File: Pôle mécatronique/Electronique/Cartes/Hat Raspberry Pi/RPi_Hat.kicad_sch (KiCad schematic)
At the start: 9 parts, among them J1 Conn_02x03_Odd_Even, U1 XBee, U2 MCP25625-x-SS, Y1 8MHz

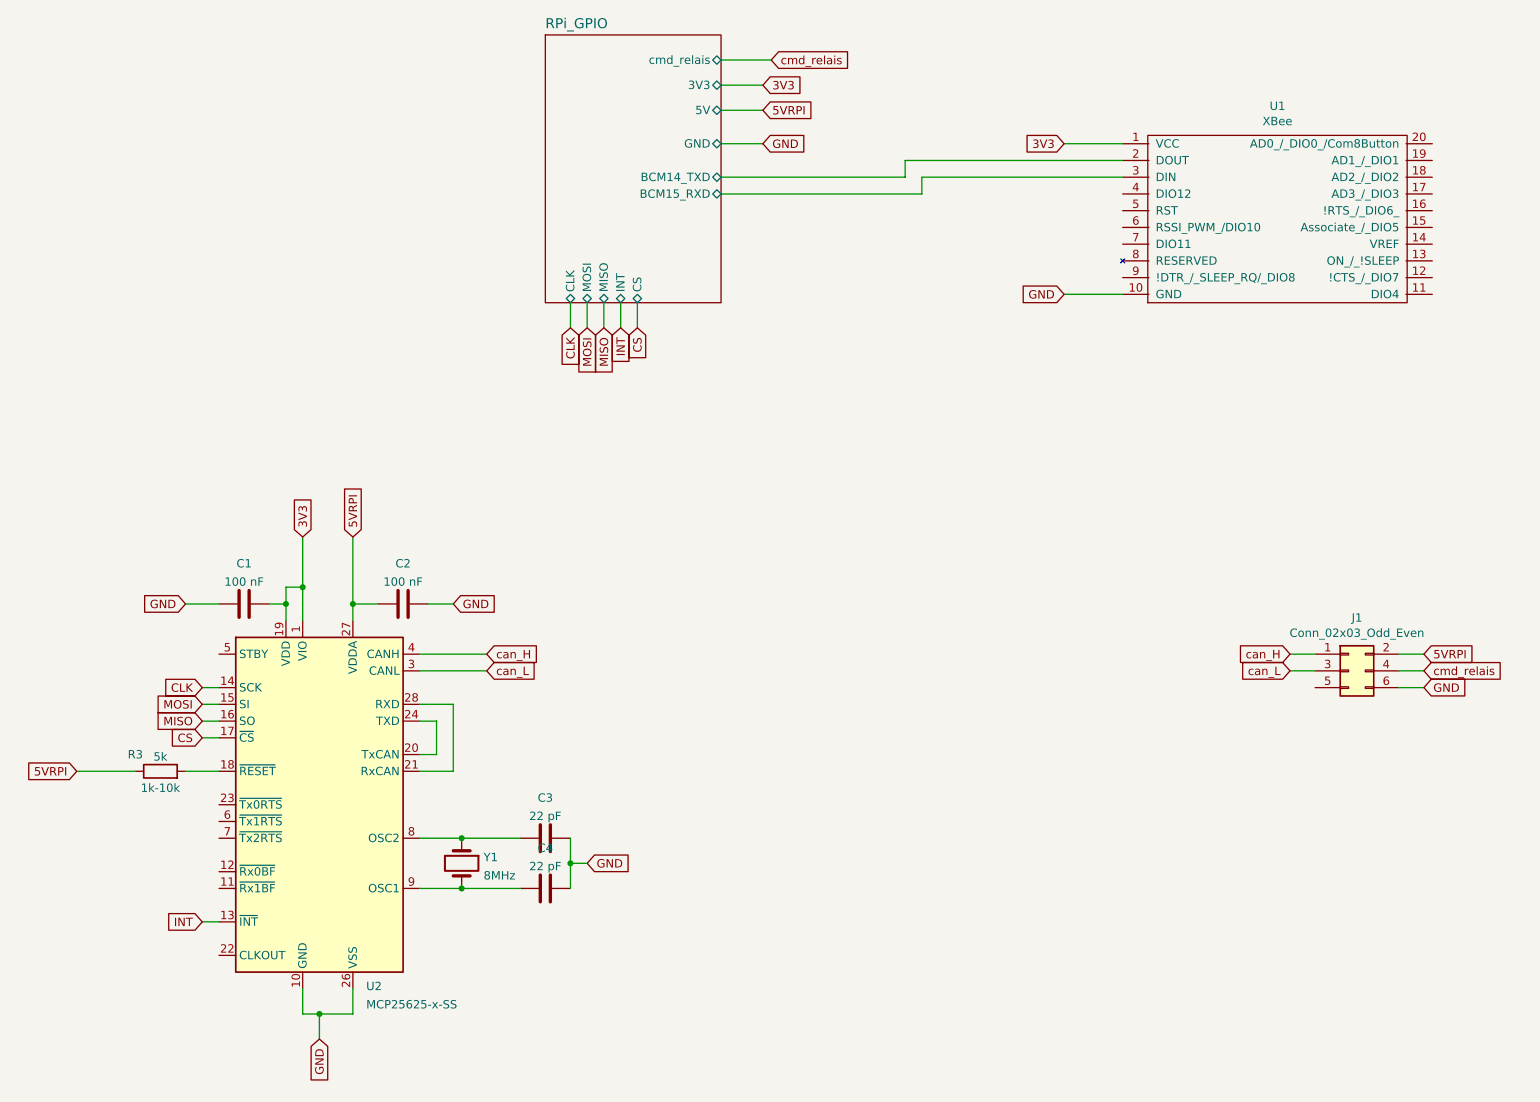
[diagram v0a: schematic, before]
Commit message: Update alim
Corrections pistes et via
Merci Hugo et Francois
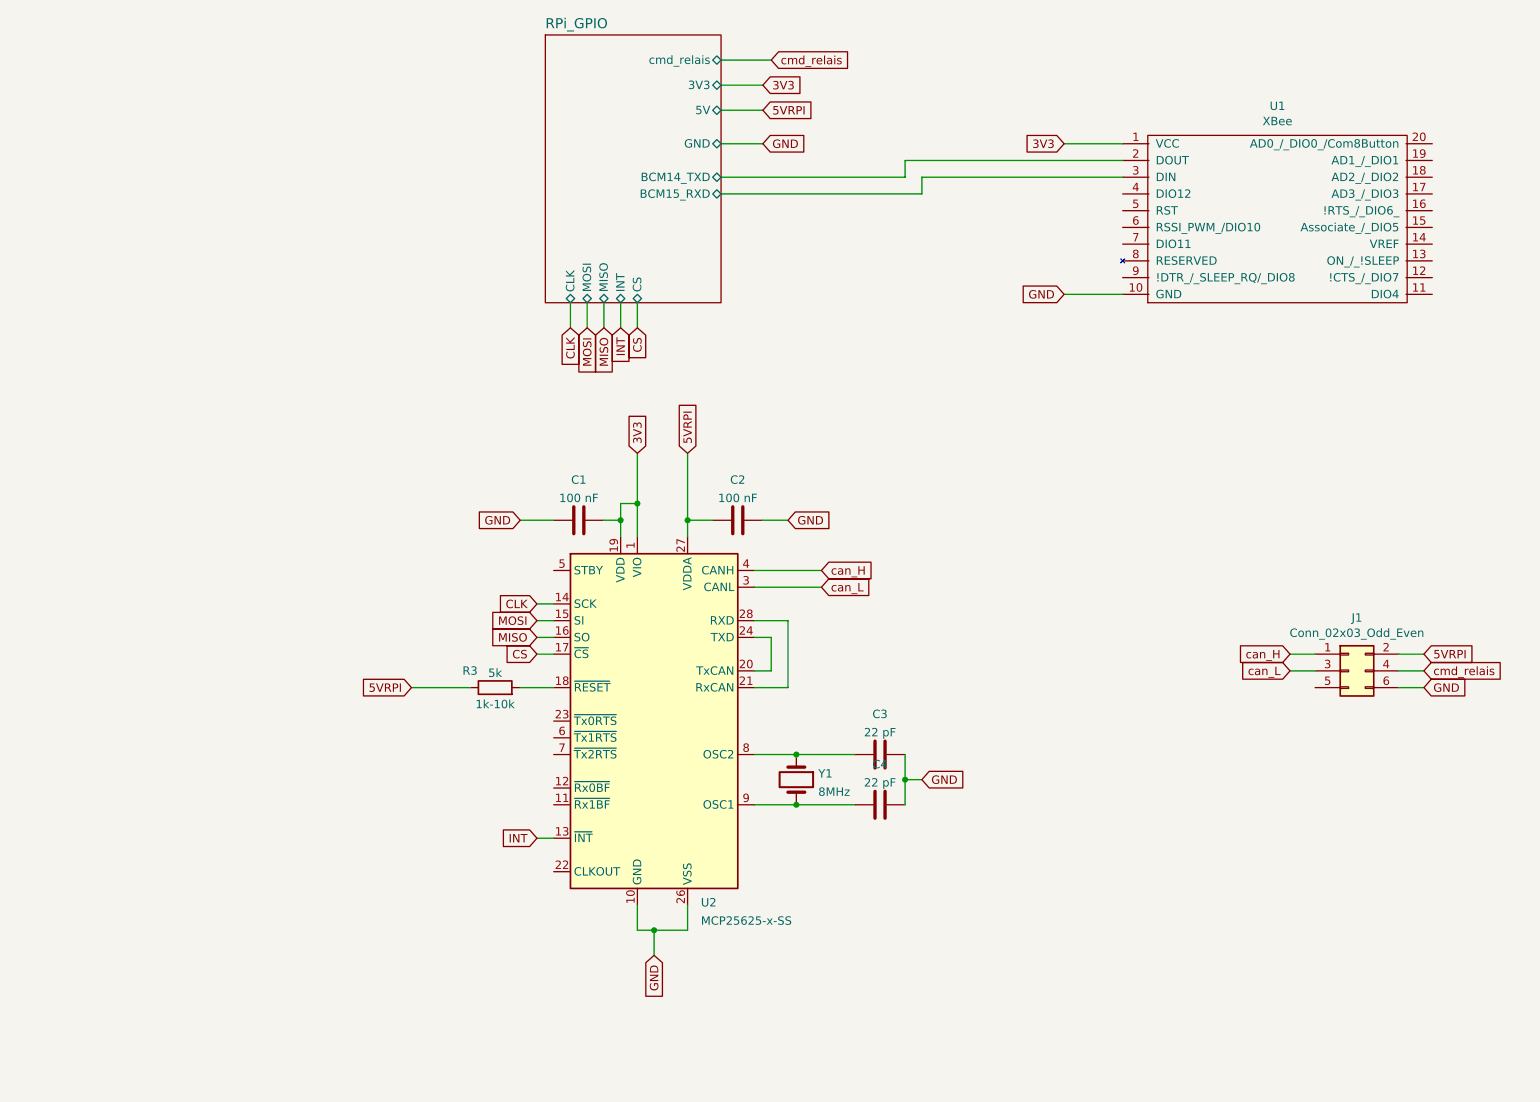
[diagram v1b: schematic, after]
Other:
- moved on the sheet: C1, C2, C3, C4, R3, U2, Y1

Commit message: Update alim correction
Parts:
- added R1: R, Resistor_THT:R_Axial_DIN0207_L6.3mm_D2.5mm_P2.54mm_Vertical, symbol Device:R
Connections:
- net can_H: now also R1.2
- net can_L: now also R1.1
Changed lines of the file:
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@@
   (junction (at 139.7 140.97) (diameter 0) (color 0 0 0 0)
   )
+  (junction (at 201.93 121.92) (diameter 0) (color 0 0 0 0)
+  )
   (junction (at 113.03 105.41) (diameter 0) (color 0 0 0 0)
   )
   (junction (at 118.11 167.64) (diameter 0) (color 0 0 0 0)
   )
+  (junction (at 201.93 129.54) (diameter 0) (color 0 0 0 0)
+  )
   (junction (at 156.21 144.78) (diameter 0) (color 0 0 0 0)
   )
@@
     (stroke (width 0) (type default) (color 0 0 0 0))
   )
+  (wire (pts (xy 201.93 121.92) (xy 209.55 121.92))
+    (stroke (width 0) (type default) (color 0 0 0 0))
+  )
   (wire (pts (xy 113.03 102.87) (xy 115.57 102.87))
     (stroke (width 0) (type default) (color 0 0 0 0))
@@
     (stroke (width 0) (type default) (color 0 0 0 0))
   )
+  (wire (pts (xy 196.85 129.54) (xy 201.93 129.54))
+    (stroke (width 0) (type default) (color 0 0 0 0))
+  )
   (wire (pts (xy 100.33 125.73) (xy 102.87 125.73))
     (stroke (width 0) (type default) (color 0 0 0 0))
@@
     (stroke (width 0) (type default) (color 0 0 0 0))
   )
+  (wire (pts (xy 196.85 121.92) (xy 201.93 121.92))
+    (stroke (width 0) (type default) (color 0 0 0 0))
+  )
   (wire (pts (xy 134.62 105.41) (xy 138.43 105.41))
     (stroke (width 0) (type default) (color 0 0 0 0))
@@
     (stroke (width 0) (type default) (color 0 0 0 0))
   )
+  (wire (pts (xy 209.55 128.27) (xy 209.55 129.54))
+    (stroke (width 0) (type default) (color 0 0 0 0))
+  )
   (wire (pts (xy 123.19 163.83) (xy 123.19 167.64))
     (stroke (width 0) (type default) (color 0 0 0 0))
@@
     (stroke (width 0) (type default) (color 0 0 0 0))
   )
+  (wire (pts (xy 209.55 125.73) (xy 218.44 125.73))
+    (stroke (width 0) (type default) (color 0 0 0 0))
+  )
   (wire (pts (xy 100.33 153.67) (xy 102.87 153.67))
     (stroke (width 0) (type default) (color 0 0 0 0))
@@
     (stroke (width 0) (type default) (color 0 0 0 0))
   )
-  (wire (pts (xy 214.63 128.27) (xy 218.44 128.27))
-    (stroke (width 0) (type default) (color 0 0 0 0))
-  )
   (wire (pts (xy 107.95 72.39) (xy 107.95 76.2))
     (stroke (width 0) (type default) (color 0 0 0 0))
@@
     (stroke (width 0) (type default) (color 0 0 0 0))
   )
+  (wire (pts (xy 218.44 128.27) (xy 209.55 128.27))
+    (stroke (width 0) (type default) (color 0 0 0 0))
+  )
   (wire (pts (xy 135.89 128.27) (xy 133.35 128.27))
     (stroke (width 0) (type default) (color 0 0 0 0))
   )
+  (wire (pts (xy 209.55 121.92) (xy 209.55 125.73))
+    (stroke (width 0) (type default) (color 0 0 0 0))
+  )
   (wire (pts (xy 128.27 48.26) (xy 134.62 48.26))
     (stroke (width 0) (type default) (color 0 0 0 0))
@@
     (stroke (width 0) (type default) (color 0 0 0 0))
   )
-  (wire (pts (xy 214.63 125.73) (xy 218.44 125.73))
-    (stroke (width 0) (type default) (color 0 0 0 0))
-  )
   (wire (pts (xy 123.19 105.41) (xy 127 105.41))
     (stroke (width 0) (type default) (color 0 0 0 0))
@@
   )
   (wire (pts (xy 139.7 140.97) (xy 148.59 140.97))
+    (stroke (width 0) (type default) (color 0 0 0 0))
+  )
+  (wire (pts (xy 201.93 129.54) (xy 209.55 129.54))
     (stroke (width 0) (type default) (color 0 0 0 0))
   )
@@
     )
   )
-  (global_label "can_L" (shape input) (at 214.63 128.27 180) (fields_autoplaced)
-    (effects (font (size 1.27 1.27)) (justify right))
-    (property "Intersheet References" "${INTERSHEET_REFS}" (id 0) (at 189.23 57.15 0)
+  (global_label "can_L" (shape input) (at 196.85 129.54 180) (fields_autoplaced)
+    (effects (font (size 1.27 1.27)) (justify right))
+    (property "Intersheet References" "${INTERSHEET_REFS}" (id 0) (at 171.45 58.42 0)
       (effects (font (size 1.27 1.27)) hide)
     )
@@
     )
   )
-  (global_label "can_H" (shape input) (at 214.63 125.73 180) (fields_autoplaced)
-    (effects (font (size 1.27 1.27)) (justify right))
-    (property "Intersheet References" "${INTERSHEET_REFS}" (id 0) (at 189.23 59.69 0)
+  (global_label "can_H" (shape input) (at 196.85 121.92 180) (fields_autoplaced)
+    (effects (font (size 1.27 1.27)) (justify right))
+    (property "Intersheet References" "${INTERSHEET_REFS}" (id 0) (at 171.45 55.88 0)
       (effects (font (size 1.27 1.27)) hide)
     )
@@
     )
     (property "Description" "1k-10k" (id 4) (at 93.98 133.35 90))
+    (pin "1")
+    (pin "2")
+  )
+  (symbol (lib_id "Device:R") (at 201.93 125.73 180) (unit 1)
+    (in_bom yes) (on_board yes) (fields_autoplaced)
+    (property "Reference" "R1" (id 0) (at 203.708 124.8215 0)
+      (effects (font (size 1.27 1.27)) (justify right))
+    )
+    (property "Value" "R" (id 1) (at 203.708 127.5966 0)
+      (effects (font (size 1.27 1.27)) (justify right))
+    )
+    (property "Footprint" "Resistor_THT:R_Axial_DIN0207_L6.3mm_D2.5mm_P2.54mm_Vertical" (id 2) (at 203.708 125.73 90)
+      (effects (font (size 1.27 1.27)) hide)
+    )
+    (property "Datasheet" "~" (id 3) (at 201.93 125.73 0)
+      (effects (font (size 1.27 1.27)) hide)
+    )
     (pin "1")
     (pin "2")
@@
       (reference "J2") (unit 1) (value "RPi_GPIO") (footprint "RPi_Hat:Pin_Header_Straight_2x20")
     )
+    (path "/5d503d09-3382-41b1-85dd-a984512b456d"
+      (reference "R1") (unit 1) (value "R") (footprint "Resistor_THT:R_Axial_DIN0207_L6.3mm_D2.5mm_P2.54mm_Vertical")
+    )
     (path "/47b96755-77b4-4d1f-b7c7-e83301b841d7"

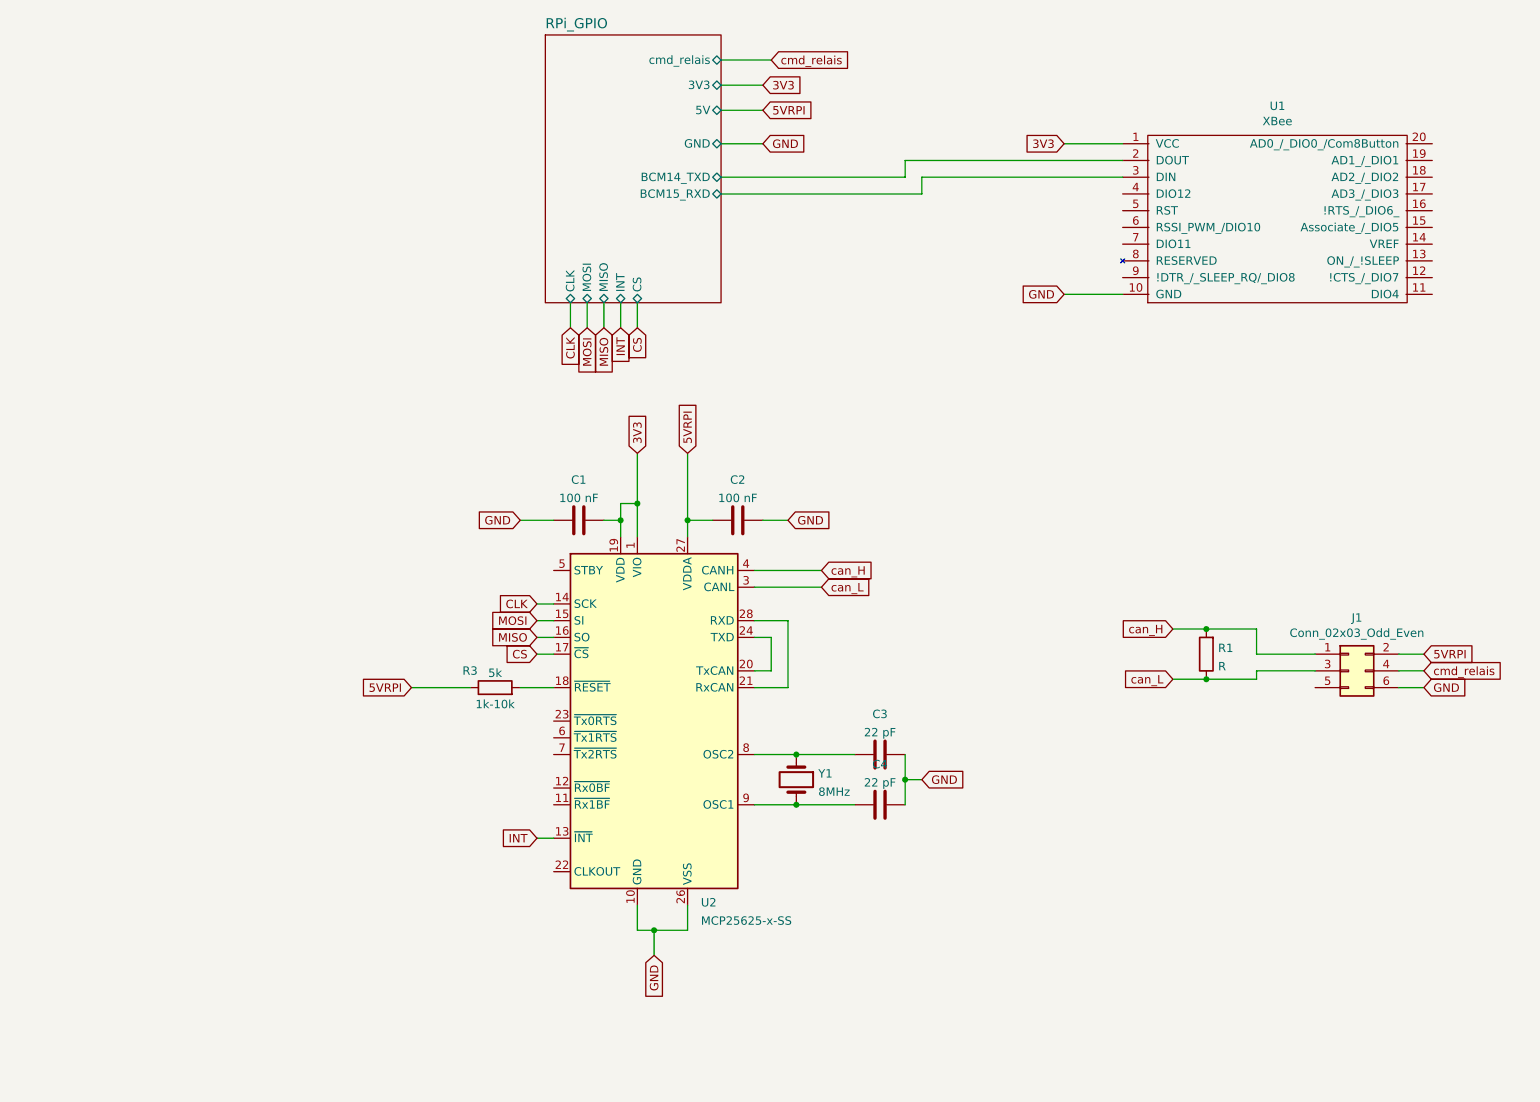
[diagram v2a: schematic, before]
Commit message: Update HAT
- Ajout des pads
- Correction du schéma
- Corrections diverses
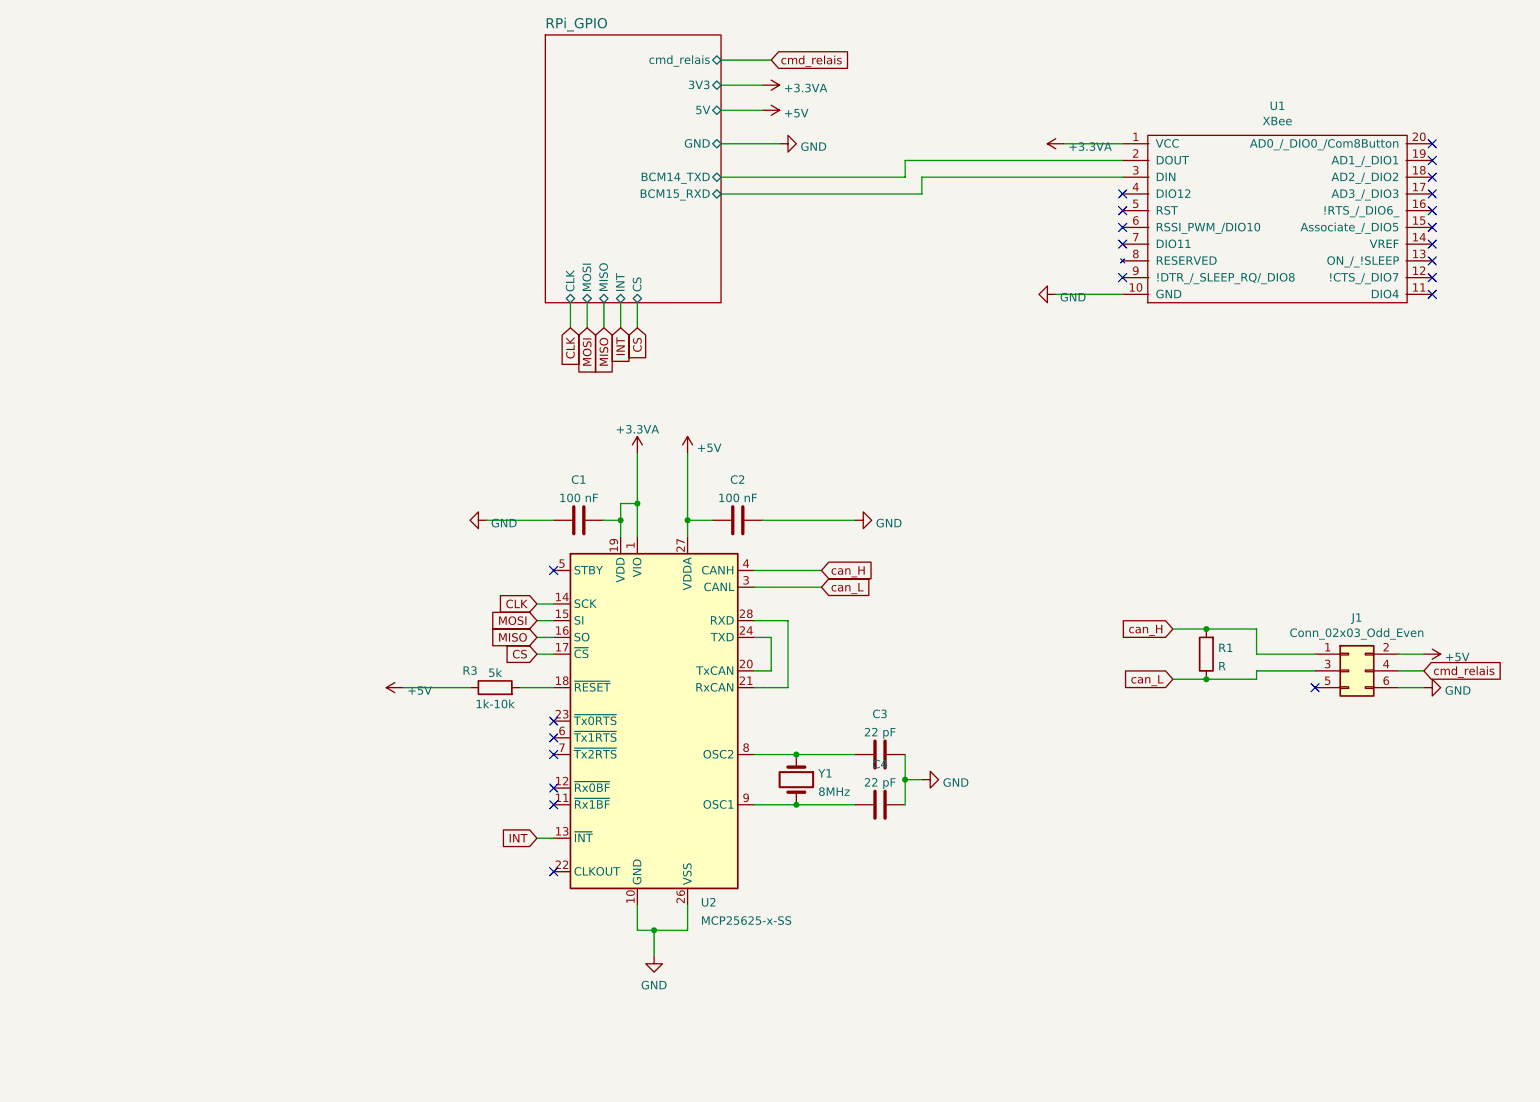
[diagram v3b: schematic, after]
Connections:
- net 3V3 renamed +3.3VA
- net 5VRPI renamed +5V
- no-connect marks 0 -> 23
